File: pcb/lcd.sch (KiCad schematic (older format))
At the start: 1 part, among them U100 MCIMX7S5EVM08SC

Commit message: pcb: working on sch
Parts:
- added C500, C501, C502, C503: 100nF, symbol Device:C
- added C504, C505, C506: 220nF, symbol Device:C
- added C507: 2.2uF, symbol Device:C
- added C508, C510, C512: 10uF, symbol Device:C
- added C509: 68nF, symbol Device:C
- added C511: 1uF, symbol Device:C
- added D500: RB521S30T1G, symbol Device:D_Schottky
- added D500: DFLS240, symbol Device:D_Schottky
- added J500: FPC_18P_1.0MM, symbol Connector_Generic:Conn_01x18
- added L500: 15uH, symbol Device:L
- added Q500: IRLML6402, Package_TO_SOT_SMD:SOT-23, symbol Transistor_FET:IRLML6402
- added R500: 100K, symbol Device:R
- added R501, R505, R506, R507, R508: 10K, symbol Device:R
- added R502: 15K, symbol Device:R
- added R503: 118K, symbol Device:R
- added R504: 2.32M, symbol Device:R
- added RN500, RN501, RN502, RN503: 33R, symbol Device:R_Pack04
- added RV500: R_POT, symbol Device:R_POT
- added U500: XC2C32A, Package_QFP:LQFP-44_10x10mm_P0.8mm, symbol symbols:XC2C32A
- added U501: ADP5075, symbol symbols:ADP5075
- added U502: LM324, symbol Amplifier_Operational:LM324
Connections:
- net labels added: +1V8, +3V3, +3V3_LCD, BT_CFG_1, BT_CFG_10, BT_CFG_11, BT_CFG_12, BT_CFG_13, BT_CFG_14, BT_CFG_2, BT_CFG_3, BT_CFG_4, BT_CFG_5, BT_CFG_6, CPLD_JTAG_TCK, CPLD_JTAG_TDI, CPLD_JTAG_TDO, CPLD_JTAG_TMS, GND, LCD_ARM_CLK, LCD_ARM_D6, LCD_ARM_D7, LCD_ARM_EN, LCD_ARM_HSYNC, LCD_ARM_VSYNC, LCD_CP, LCD_CPG, LCD_CPL, LCD_D0, LCD_D1, LCD_FR, LCD_RESET, LCD_S, LCD_ST, LCD_V1, LCD_V2, LCD_V3, LCD_V4, LCD_V5, PMIC_STBY_REQ
- wire segments 6 -> 199
- no-connect marks 0 -> 40
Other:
- note added: "-15V"
- note added: "TFT to STN Bridge"

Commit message: pcb: draw sch for wifi & bt
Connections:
- net labels added: LCD_PWR_EN
- net labels removed: PMIC_STBY_REQ
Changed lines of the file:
@@
 $Descr A4 11693 8268
 encoding utf-8
-Sheet 6 10
+Sheet 6 11
 Title "STN LCD"
 Date ""
@@
 Wire Wire Line
 	9400 1100 9400 2900
-$Comp
-L power:+3V3 #PWR?
-U 1 1 5D4C2328
-P 9300 1000
-F 0 "#PWR?" H 9300 850 50  0001 C CNN
-F 1 "+3V3" H 9315 1173 50  0000 C CNN
-F 2 "" H 9300 1000 50  0001 C CNN
-F 3 "" H 9300 1000 50  0001 C CNN
-	1    9300 1000
-	1    0    0    -1
-$EndComp
 Text Label 8900 1200 0    50   ~ 0
 LCD_CPG
@@
 $EndComp
 Text GLabel 4400 4900 0    50   Input ~ 0
-PMIC_STBY_REQ
+LCD_PWR_EN
 Wire Wire Line
 	4900 4800 4900 4900
@@
 	5800 7000 5800 7100
 Connection ~ 6400 6400
-Text Label 9050 6400 0    50   ~ 0
+Text Label 9050 4950 0    50   ~ 0
 LCD_V1
 Text Notes 6750 6350 0    50   ~ 0
@@
 	9400 6400 7200 6400
 Connection ~ 7200 6400
-$Comp
-L power:GND #PWR?
-U 1 1 5D75F54C
-P 7200 4500
-F 0 "#PWR?" H 7200 4250 50  0001 C CNN
-F 1 "GND" H 7205 4327 50  0000 C CNN
-F 2 "" H 7200 4500 50  0001 C CNN
-F 3 "" H 7200 4500 50  0001 C CNN
-	1    7200 4500
-	-1   0    0    1
-$EndComp
 Wire Wire Line
 	7200 6050 7200 6000
@@
 	9400 4950 8400 4950
 Connection ~ 8400 4950
-Text Label 9050 6150 0    50   ~ 0
+Text Label 9050 5350 0    50   ~ 0
 LCD_V2
 Text Label 9050 5750 0    50   ~ 0
 LCD_V3
-Text Label 9050 5350 0    50   ~ 0
+Text Label 9050 6150 0    50   ~ 0
 LCD_V4
-Text Label 9050 4950 0    50   ~ 0
+Text Label 9050 6400 0    50   ~ 0
 LCD_V5
 $Comp
@@
 Wire Wire Line
 	6700 4500 7200 4500
-Connection ~ 7200 4500
 Wire Wire Line
 	1400 7300 1600 7300
+$Comp
+L symbols:+3V3_LCD #PWR?
+U 1 1 5D1B9280
+P 6700 4500
+F 0 "#PWR?" H 6700 4350 50  0001 C CNN
+F 1 "+3V3_LCD" H 6715 4673 50  0000 C CNN
+F 2 "" H 6700 4500 50  0001 C CNN
+F 3 "" H 6700 4500 50  0001 C CNN
+	1    6700 4500
+	1    0    0    -1
+$EndComp
+Connection ~ 6700 4500
+$Comp
+L symbols:+3V3_LCD #PWR?
+U 1 1 5D1B9CC5
+P 9300 1000
+F 0 "#PWR?" H 9300 850 50  0001 C CNN
+F 1 "+3V3_LCD" H 9315 1173 50  0000 C CNN
+F 2 "" H 9300 1000 50  0001 C CNN
+F 3 "" H 9300 1000 50  0001 C CNN
+	1    9300 1000
+	1    0    0    -1
+$EndComp
 $EndSCHEMATC

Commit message: pcb: working on sch
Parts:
- added R504: 10K, symbol Device:R
- R503: value 118K -> 100K
- R506: value 10K -> 75K
- RV500: value R_POT -> 100K
- renumbered R504 to R509
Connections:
- wire segments 199 -> 203
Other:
- note added: "-8.5V to -17.8V"
- note removed: "-15V"
- moved on the sheet: C511, RV500

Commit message: pcb: finishing sch for r0.1
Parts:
- C500, C501, C502, C503, C504, C505, C506, C507, C509, C511: footprint (none) -> Capacitor_SMD:C_0402_1005Metric
- C508, C510, C512: footprint (none) -> Capacitor_SMD:C_0603_1608Metric
- D500: footprint (none) -> Diode_SMD:D_SOD-523
- D500: footprint (none) -> Diode_SMD:D_SOD-123
- J500: footprint (none) -> Connector_FFC-FPC:TE_1-84953-8_1x18-1MP_P1.0mm_Horizontal
- L500: footprint (none) -> Inductor_SMD:L_Vishay_IHLP-4040
- R500, R501, R502, R503, R504, R505, R506, R507, R508, R509: footprint (none) -> Resistor_SMD:R_0603_1608Metric
- RN500, RN501, RN502, RN503: footprint (none) -> Resistor_SMD:R_Array_Convex_4x0402
- RV500: value 100K -> RK14J11A0A02; footprint (none) -> footprints:Potentiometer_RK14J
- U100: footprint (none) -> footprints:BGA-541_25x25_19.0x19.0mm
- U501: footprint (none) -> footprints:WLCSP-12_3x4
- U502: footprint (none) -> Package_SO:SOIC-16_3.9x9.9mm_P1.27mm
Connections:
- net labels added: ~LCD_PWR_EN
- net labels removed: LCD_PWR_EN
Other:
- note added: "-11.6V to -17.8V"
- note removed: "-8.5V to -17.8V"

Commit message: pcb: initial netlist
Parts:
- renumbered D500 to D501
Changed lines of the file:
@@
 $EndComp
 $Comp
-L Device:D_Schottky D500
+L Device:D_Schottky D501
 U 1 1 5D685CDF
 P 6150 6600
-F 0 "D500" H 5950 6650 50  0000 C CNN
+F 0 "D501" H 5950 6650 50  0000 C CNN
 F 1 "DFLS240" H 6400 6650 50  0000 C CNN
 F 2 "Diode_SMD:D_SOD-123" H 6150 6600 50  0001 C CNN

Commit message: pcb: working on layout
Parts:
- removed U500: XC2C32A, Package_QFP:LQFP-44_10x10mm_P0.8mm, symbol symbols:XC2C32A
- added U500: XC2C32A_QF32, Package_DFN_QFN:QFN-32-1EP_5x5mm_P0.5mm_EP3.1x3.1mm, symbol symbols:XC2C32A_QF32
- L500: footprint Inductor_SMD:L_Vishay_IHLP-4040 -> Inductor_SMD:L_Vishay_IHLP-1212
- U502: footprint Package_SO:SOIC-16_3.9x9.9mm_P1.27mm -> Package_SO:TSSOP-14_4.4x5mm_P0.65mm
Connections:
- net labels added: SW_A, SW_B, SW_DN, SW_LE, SW_RI, SW_SE, SW_ST, SW_UP
- wire segments 203 -> 208
- no-connect marks 40 -> 32
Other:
- moved on the sheet: C500, C501, C502, C503, J500, RN502, RN503

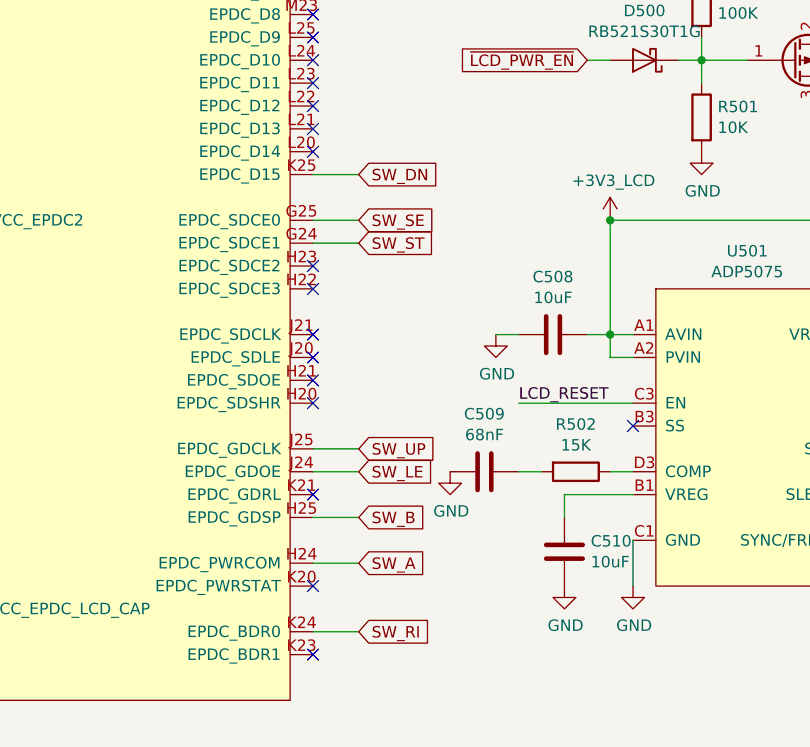
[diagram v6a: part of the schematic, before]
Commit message: pcb: add board outline
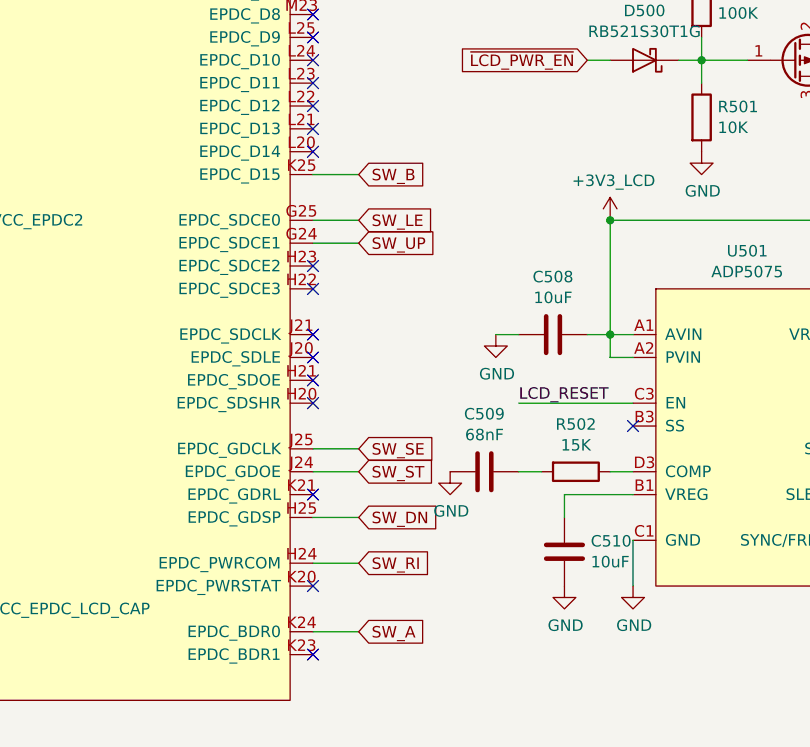
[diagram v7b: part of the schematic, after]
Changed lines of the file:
@@
 Wire Wire Line
 	3200 5400 3400 5400
+Text GLabel 3400 6900 2    50   Input ~ 0
+SW_DN
+Text GLabel 3400 6600 2    50   Input ~ 0
+SW_SE
+Text GLabel 3400 6700 2    50   Input ~ 0
+SW_ST
+Text GLabel 3400 5700 2    50   Input ~ 0
+SW_UP
+Text GLabel 3400 5600 2    50   Input ~ 0
+SW_LE
+Text GLabel 3400 7400 2    50   Input ~ 0
+SW_A
+Text GLabel 3400 7100 2    50   Input ~ 0
+SW_RI
 Text GLabel 3400 5400 2    50   Input ~ 0
-SW_DN
-Text GLabel 3400 5600 2    50   Input ~ 0
-SW_SE
-Text GLabel 3400 5700 2    50   Input ~ 0
-SW_ST
-Text GLabel 3400 6600 2    50   Input ~ 0
-SW_UP
-Text GLabel 3400 6700 2    50   Input ~ 0
-SW_LE
-Text GLabel 3400 6900 2    50   Input ~ 0
 SW_B
-Text GLabel 3400 7100 2    50   Input ~ 0
-SW_A
-Text GLabel 3400 7400 2    50   Input ~ 0
-SW_RI
 $EndSCHEMATC

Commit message: pcb: routing
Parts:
- C500, C501, C502, C503, C504, C505, C506, C507, C508, C509, C510, C511, C512: symbol Device:C -> pcb-rescue:C-Device
- D500, D501: symbol Device:D_Schottky -> pcb-rescue:D_Schottky-Device
- J500: symbol Connector_Generic:Conn_01x18 -> pcb-rescue:Conn_01x18-Connector_Generic
- L500: symbol Device:L -> pcb-rescue:L-Device
- Q500: symbol Transistor_FET:IRLML6402 -> pcb-rescue:IRLML6402-Transistor_FET
- R500, R501, R502, R503, R504, R505, R506, R507, R508, R509: symbol Device:R -> pcb-rescue:R-Device
- RN500, RN501, RN502, RN503: symbol Device:R_Pack04 -> pcb-rescue:R_Pack04-Device
- RV500: symbol Device:R_POT -> pcb-rescue:R_POT-Device
- U502: symbol Amplifier_Operational:LM324 -> pcb-rescue:LM324-Amplifier_Operational
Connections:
- net labels added: HOLD
- wire segments 208 -> 210
- no-connect marks 32 -> 31
